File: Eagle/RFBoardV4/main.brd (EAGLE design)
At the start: 34.3 x 77.5 mm, 31 parts, among them Q1 8/16/20MHz, U1 ATMEGA328

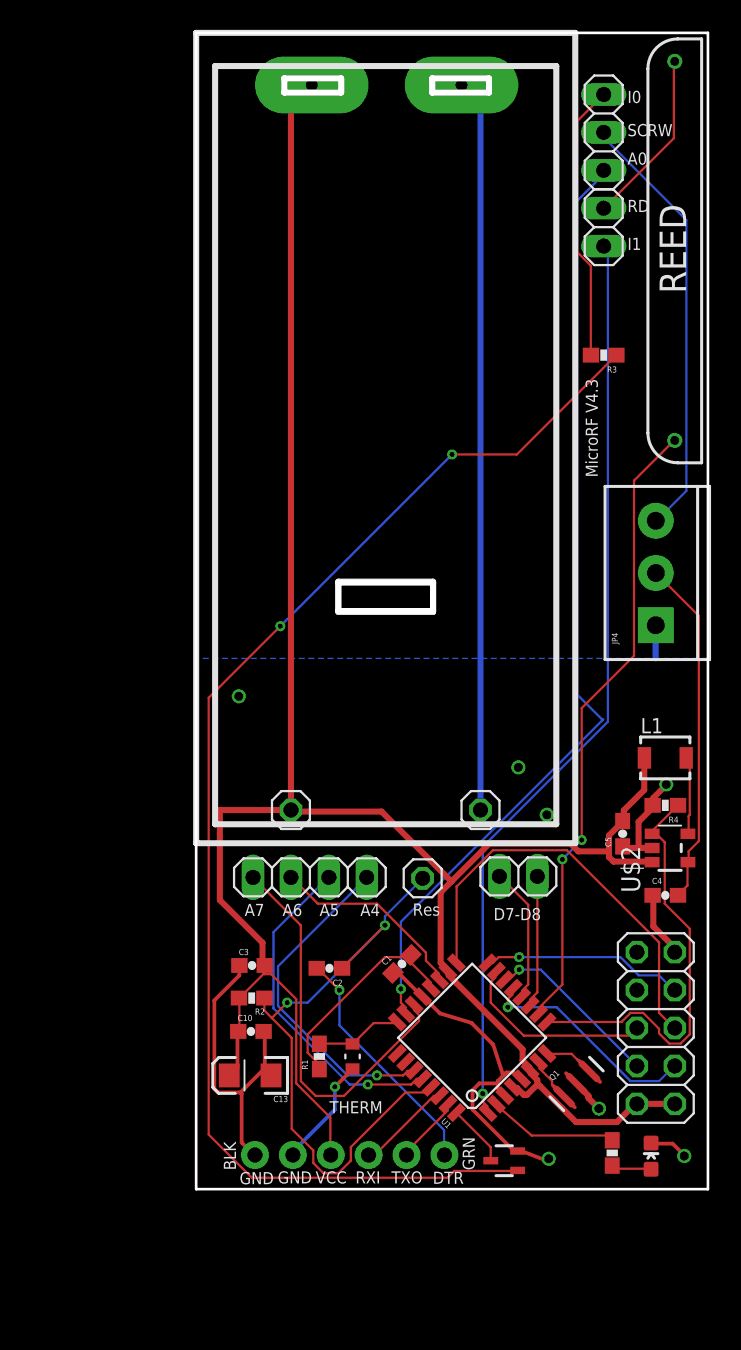
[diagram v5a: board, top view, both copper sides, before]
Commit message: 4.3 checked in
- Reed can now be connected to either interrupt
- Fixed pads for the 3.3 boost circuit
- General improvements
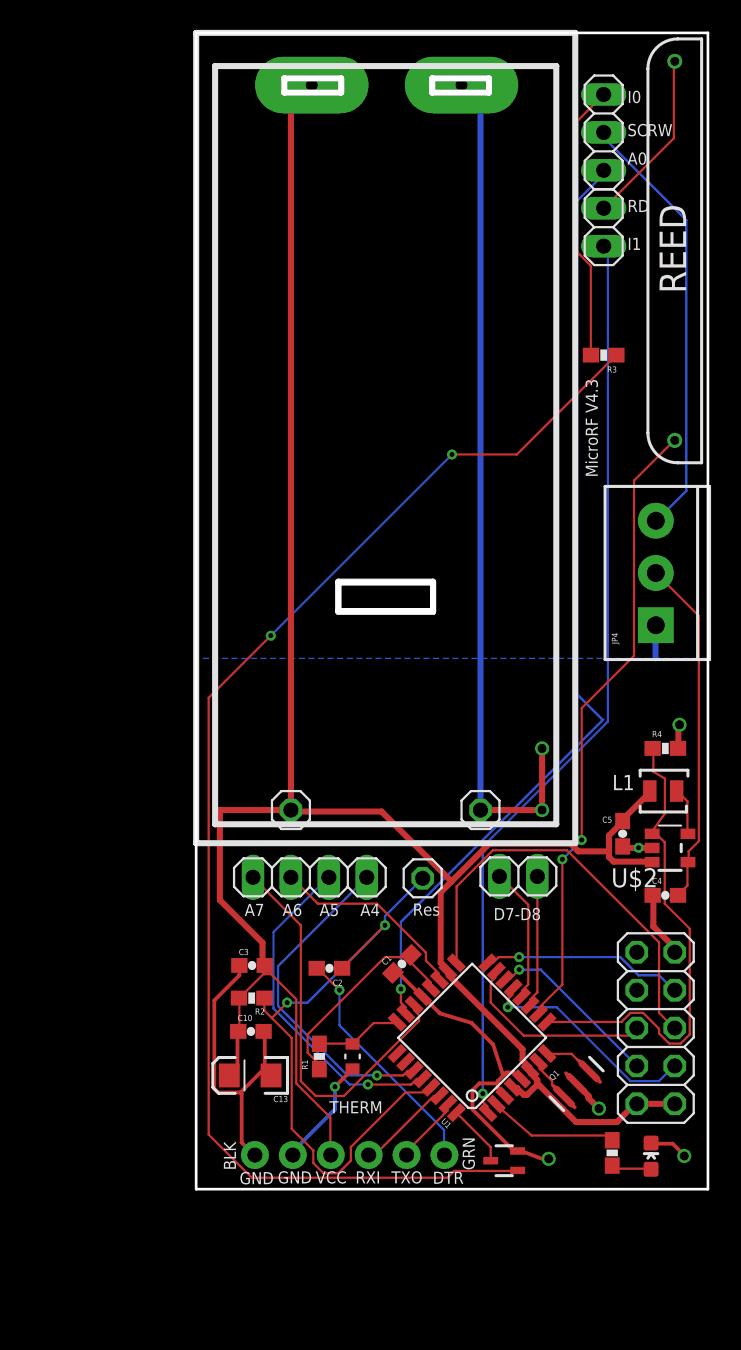
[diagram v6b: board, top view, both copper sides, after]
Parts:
- L1: value VLF302510MT -> VLF302512MT; device inductor-tdk:VLF302510MT -> inductor-tdk:VLF302512MT
- moved R4 3.81 mm to (31.4, 29.5), turned to 0 degrees
- moved L1 2.31 mm to (30.8, 26.7)
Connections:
- removed net D2: T1.1
- net D2_INT0: now also T1.1
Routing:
- net GND: track 121.0 -> 126.0 mm
- net D2_INT0: track 0.00 -> 4.18 mm
- net D2: track 4.15 -> 0.00 mm
- net D5: track 28.6 -> 32.4 mm
- net N$8: track 5.23 -> 3.19 mm
- net VCC: track 154.0 -> 152.0 mm

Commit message: Minor updates moving from 4.3 to 4.4
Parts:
- removed R4: 10K, SparkFun:0603-RES
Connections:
- net D5: no longer R4.1
- net GND: no longer R4.2
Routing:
- net D5: track 32.4 -> 26.0 mm
- net GND: track 126.0 -> 124.3 mm, vias 8 -> 7
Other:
- board text added: "MicroRF V4.4"
- board text removed: "MicroRF V4.3"
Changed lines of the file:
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@@
 <?xml version="1.0" encoding="utf-8"?>
 <!DOCTYPE eagle SYSTEM "eagle.dtd">
-<eagle version="7.5.0">
+<eagle version="7.2.0">
 <drawing>
 <settings>
@@
 <text x="32.8295" y="60.0075" size="1.778" layer="21" rot="R90">REED</text>
 <text x="15.8496" y="0.3556" size="0.8128" layer="21" font="fixed" ratio="15">DTR</text>
-<text x="26.0985" y="54.2925" size="0.8128" layer="21" ratio="15" rot="R270">MicroRF V4.3</text>
+<text x="26.0985" y="54.2925" size="0.8128" layer="21" ratio="15" rot="R270">MicroRF V4.4</text>
 <text x="31.0515" y="4.7625" size="0.8128" layer="22" ratio="15" rot="MR90">VCC</text>
 <text x="31.877" y="17.018" size="0.8128" layer="22" ratio="15" rot="MR270">GND</text>
@@
 <element name="R3" library="SparkFun" package="0603-RES" value="10K" x="27.305" y="55.88" rot="R180"/>
 <element name="JP4" library="SparkFun-Connectors" package="SCREWTERMINAL-3.5MM-3" value="" x="30.7975" y="37.7825" rot="R90"/>
-<element name="R4" library="SparkFun" package="0603-RES" value="10K" x="31.4325" y="29.5275"/>
 <element name="U$1" library="battery_wilkie" package="AAABATTERY" value="BAT" x="1.27" y="75.2475"/>
 <element name="U$2" library="boost" package="SOT23-5" value="XC9140" x="31.75" y="22.86" smashed="yes" rot="R90">
@@
 </polygon>
 <via x="26.9875" y="5.3975" extent="1-16" drill="0.6"/>
-<via x="32.385" y="31.115" extent="1-16" drill="0.6"/>
 <via x="32.7025" y="2.2225" extent="1-16" drill="0.6"/>
 <contactref element="GND" pad="1"/>
@@
 <wire x1="6.477" y1="2.5146" x2="6.477" y2="2.286" width="0.254" layer="16"/>
 <via x="9.2964" y="6.858" extent="1-16" drill="0.3302"/>
-<contactref element="R4" pad="2"/>
 <wire x1="6.477" y1="2.286" x2="6.426178125" y2="2.3368" width="0.4064" layer="16"/>
 <wire x1="23.4696" y1="1.905" x2="23.4569" y2="1.9177" width="0.1524" layer="1"/>
@@
 <wire x1="28.575" y1="22.9362" x2="28.6512" y2="22.86" width="0.4064" layer="1"/>
 <wire x1="28.575" y1="22.9362" x2="28.575" y2="22.9625" width="0.4064" layer="1"/>
-<wire x1="32.2326" y1="29.5656" x2="32.2825" y2="29.5275" width="0.4064" layer="1"/>
 <wire x1="29.6418" y1="22.8727" x2="29.6418" y2="22.86" width="0.4064" layer="1"/>
 <via x="29.6418" y="22.8727" extent="1-16" drill="0.3302"/>
-<wire x1="32.3088" y1="31.0134" x2="32.3088" y2="29.718" width="0.4064" layer="1"/>
-<wire x1="32.385" y1="31.0896" x2="32.3088" y2="31.0134" width="0.4064" layer="1"/>
-<wire x1="32.3088" y1="29.718" x2="32.2825" y2="29.5275" width="0.4064" layer="1"/>
-<wire x1="32.385" y1="31.0896" x2="32.385" y2="31.115" width="0.4064" layer="1"/>
+<wire x1="23.1775" y1="29.5275" x2="30.7848" y2="35.56" width="0" layer="19" extent="16-16"/>
+<wire x1="28.575" y1="22.9625" x2="23.1775" y2="25.4" width="0" layer="19" extent="1-1"/>
+<wire x1="30.5825" y1="19.685" x2="30.55" y2="22.86" width="0" layer="19" extent="1-1"/>
+<wire x1="29.5275" y1="15.875" x2="30.6324" y2="17.6022" width="0" layer="19" extent="1-1"/>
+<wire x1="24.780359375" y1="7.76628125" x2="29.5275" y2="15.875" width="0" layer="19" extent="1-1"/>
+<wire x1="21.808884375" y1="7.393428125" x2="24.780359375" y2="7.76628125" width="0" layer="19" extent="1-1"/>
+<wire x1="30.48" y1="3.0868" x2="26.9875" y2="5.3975" width="0" layer="19" extent="1-1"/>
+<wire x1="10.4775" y1="8.0518" x2="15.0876" y2="12.954" width="0" layer="19" extent="1-1"/>
+<wire x1="4.0386" y1="2.286" x2="6.426178125" y2="2.3368" width="0" layer="19" extent="16-16"/>
 </signal>
 <signal name="AREF">
@@
 <signal name="D5">
 <contactref element="U1" pad="9"/>
-<contactref element="R4" pad="1"/>
 <contactref element="U$2" pad="1"/>
 <wire x1="28.4988" y1="11.2014" x2="23.5458" y2="11.2014" width="0.1524" layer="1"/>
@@
 <wire x1="23.5458" y1="11.2014" x2="23.505940625" y2="11.2013375" width="0.1524" layer="1"/>
 <wire x1="30.6324" y1="24.003" x2="30.55" y2="23.81" width="0.1524" layer="1"/>
-<wire x1="30.6324" y1="27.9654" x2="30.6324" y2="29.4894" width="0.1524" layer="1"/>
-<wire x1="31.4071" y1="27.5082" x2="30.6324" y2="27.9654" width="0.1524" layer="1"/>
-<wire x1="31.4071" y1="25.1714" x2="31.4071" y2="27.5082" width="0.1524" layer="1"/>
-<wire x1="30.6324" y1="24.0792" x2="31.4071" y2="25.1714" width="0.1524" layer="1"/>
-<wire x1="30.6324" y1="29.4894" x2="30.5825" y2="29.5275" width="0.1524" layer="1"/>
-<wire x1="30.6324" y1="24.0792" x2="30.55" y2="23.81" width="0.1524" layer="1"/>
 </signal>
 <signal name="D2_VIA_FET">

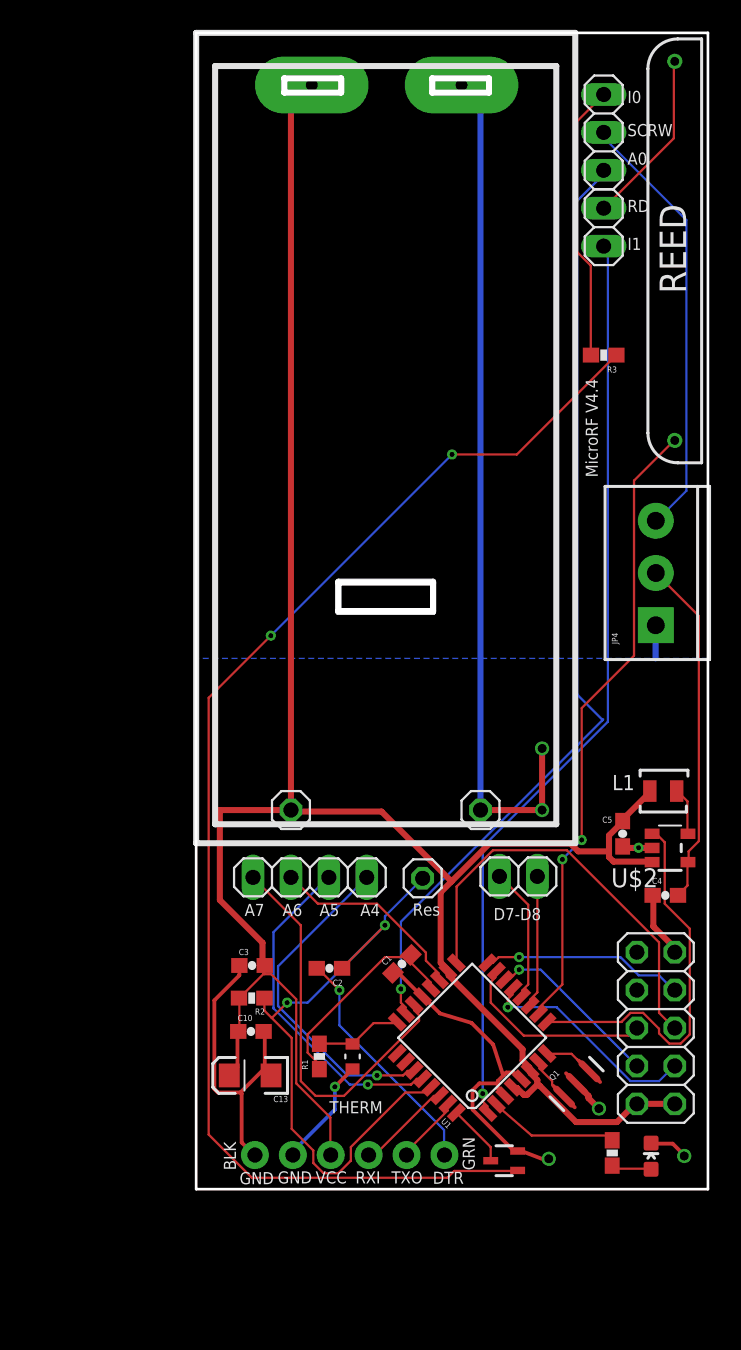
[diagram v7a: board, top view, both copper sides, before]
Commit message: Added external power option
- Added option for micro USB B for external power
- Added option for 3.3v linear regulator
- Added option for power input screw terminal
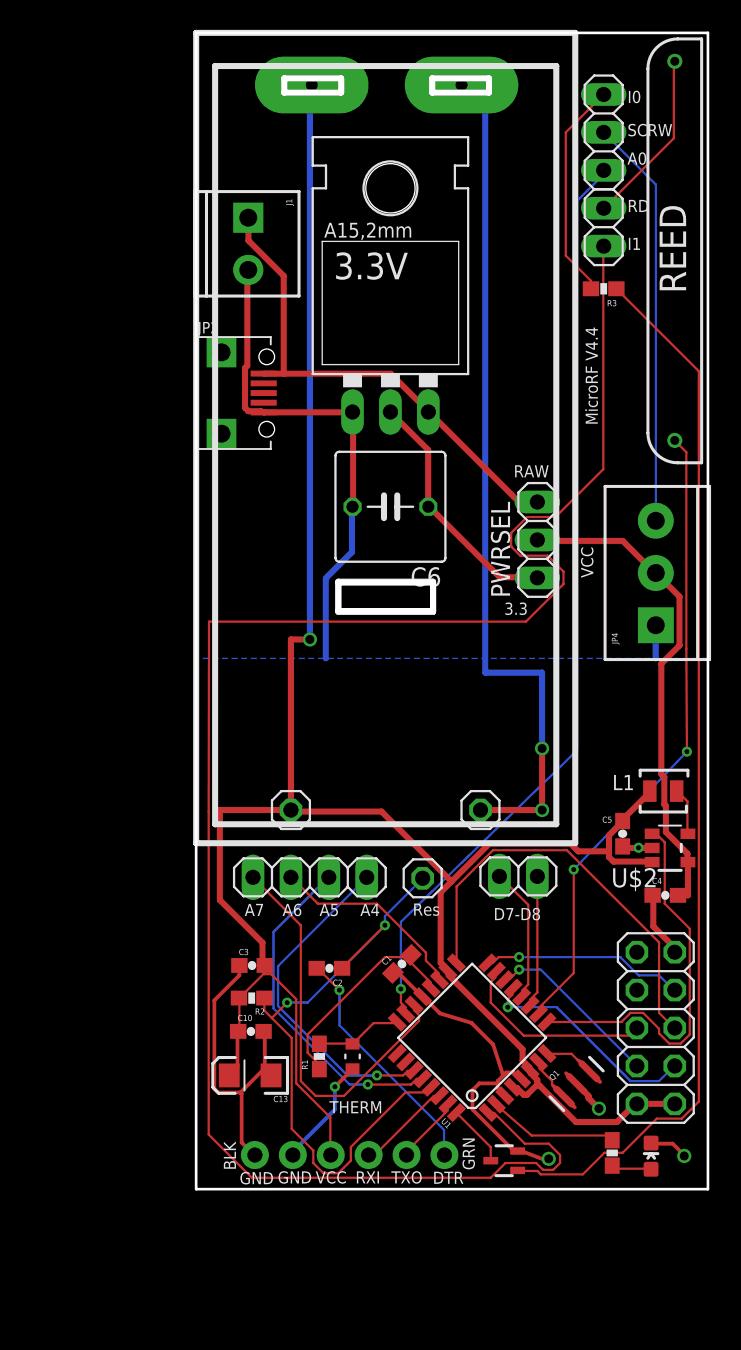
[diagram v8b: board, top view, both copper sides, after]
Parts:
- added 3.3V: LD117V33, v-reg:TO220L1
- added C6: (no value), rcl:C050-075X075
- added J1: (no value), SparkFun-Connectors:SCREWTERMINAL-3.5MM-2
- added JP2: USB-RECEPTABLE, daspilker:FCI-10103594-0001LF
- added PWRSEL: (no value), pinhead:1X03
- moved R3 4.45 mm to (27.3, 60.3)
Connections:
- new net 3.3V: 3.3V.2, C6.1, PWRSEL.1
- new net RAW_PWR: 3.3V.3, J1.1, JP2.1, PWRSEL.3
- net GND: now also 3.3V.1, C6.2, J1.2, JP2.5
- net REG_3.3V: now also PWRSEL.2
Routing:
- net D3_INT1: track 61.8 -> 120.1 mm, vias 1 -> 0
- net GND: track 124.3 -> 158.3 mm
- net RAW_PWR: track 0.00 -> 33.4 mm
- net N$6: track 88.2 -> 71.0 mm, vias 2 -> 0
- net 3.3V: track 0.00 -> 16.7 mm
- net REG_3.3V: track 23.4 -> 33.0 mm
- net D2_VIA_FET: track 18.6 -> 14.8 mm
- net SCREW_TERM: track 29.2 -> 27.5 mm
- net A0: track 64.1 -> 63.0 mm
- net REED/D6: track 42.2 -> 42.8 mm
- net VCC: vias 0 -> 1
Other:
- board text added: "3.3"
- board text added: "RAW"
- board text removed: "3V (VCC)"
